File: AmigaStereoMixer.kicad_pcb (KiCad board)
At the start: 2 copper layers, 49.3 x 55.4 mm, 16 parts, among them J1 IN1_R, J2 IN1_L, J3 IN2_L, J4 IN2_R, J5 OUT_TRS

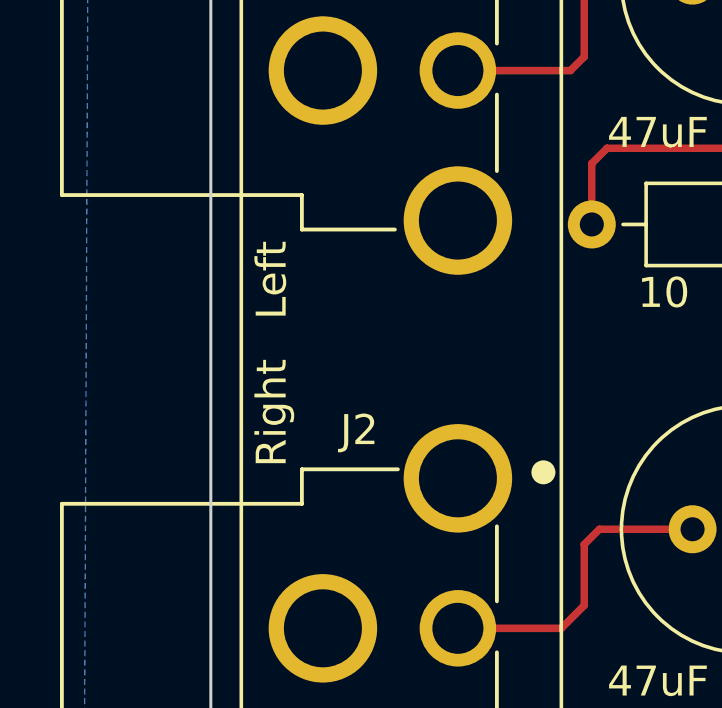
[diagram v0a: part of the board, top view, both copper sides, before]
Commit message: Arrange left & right groups more clearly in schema
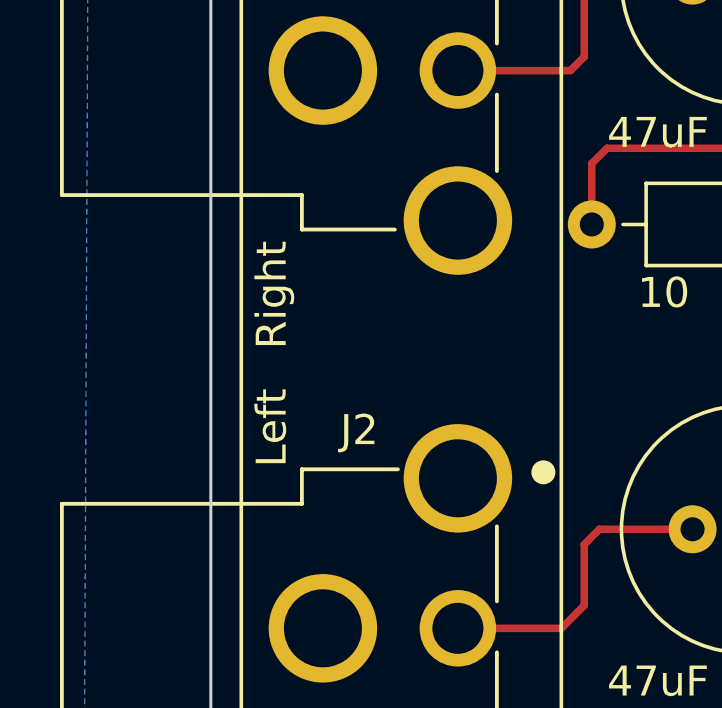
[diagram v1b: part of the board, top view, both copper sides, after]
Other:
- board text removed: "Right Left"
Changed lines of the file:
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@@
     (effects (font (size 1 1) (thickness 0.2)))
   )
-  (gr_text "Right   Left" (at 28.702 37.846 90) (layer F.SilkS)
+  (gr_text "Left   Right" (at 28.702 37.846 90) (layer F.SilkS)
     (effects (font (size 1 1) (thickness 0.2)))
   )

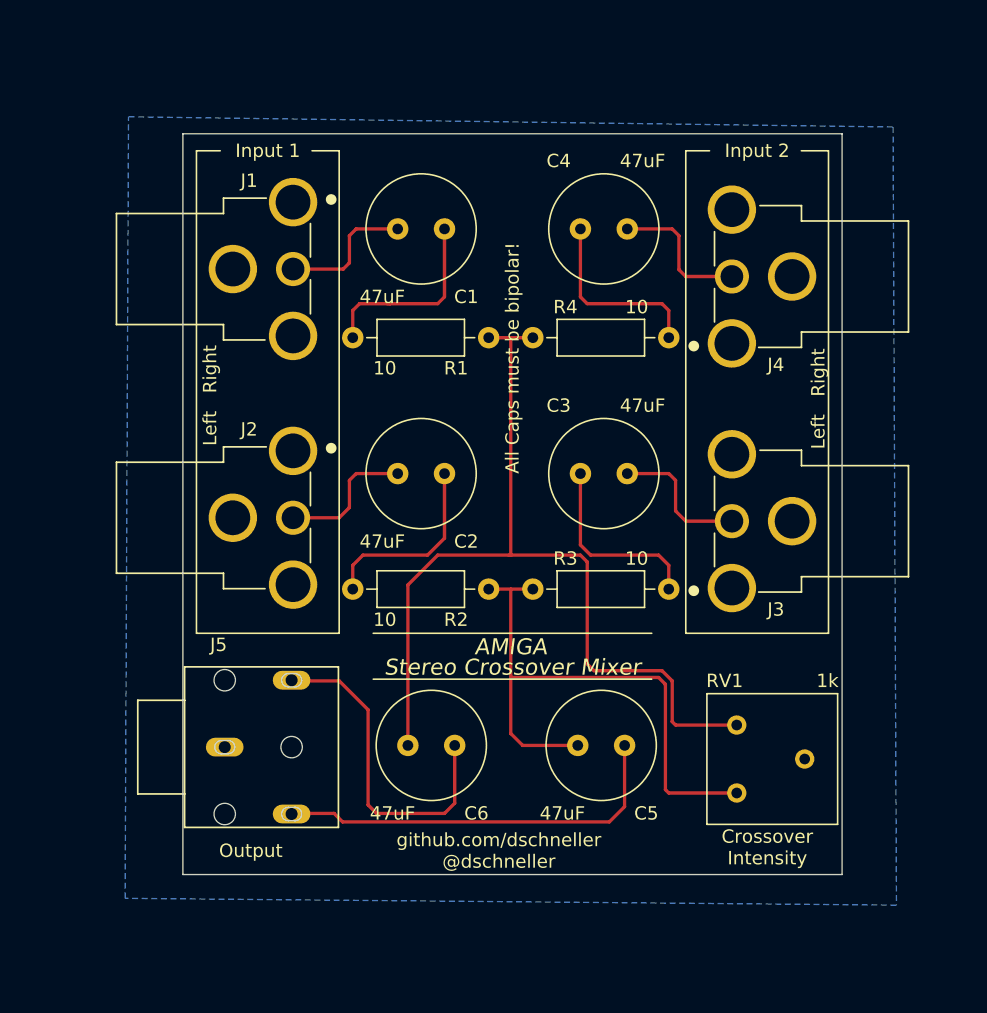
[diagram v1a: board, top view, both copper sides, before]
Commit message: Add mounting holes and an open hardware logo
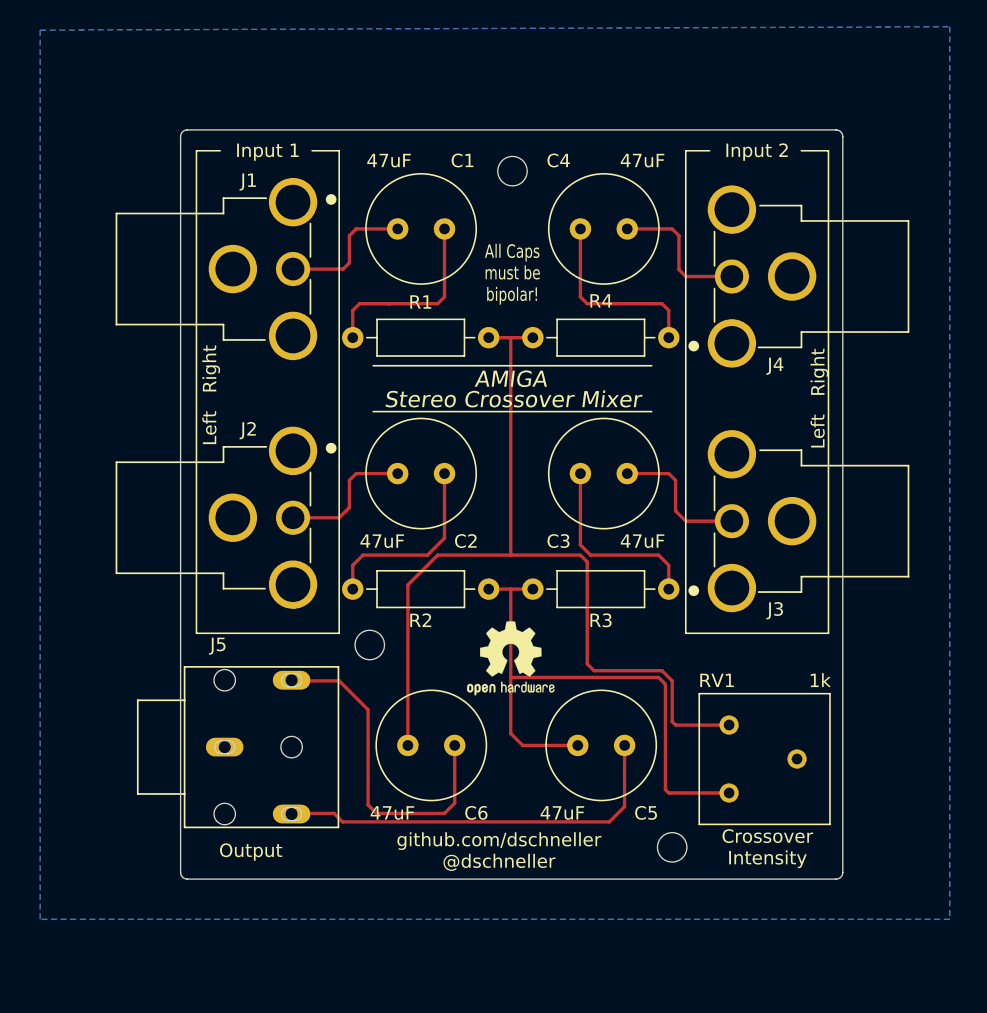
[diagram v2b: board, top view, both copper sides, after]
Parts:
- added H1: MountingHole, MountingHole:MountingHole_2.2mm_M2_DIN965, F.Cu at (51.3, 21.1)
- added H2: MountingHole, MountingHole:MountingHole_2.2mm_M2_DIN965, F.Cu at (63.2, 71.6)
- added H3: MountingHole, MountingHole:MountingHole_2.2mm_M2_DIN965, F.Cu at (40.6, 56.5)
- added REF**: OSHW-Logo2_7.3x6mm_SilkScreen, Symbol:OSHW-Logo2_7.3x6mm_SilkScreen, F.Cu at (51.2, 57.5)
- R1, R2, R3, R4: footprint AmigaStereoMixer:R_Axial_DIN0207_L6.3mm_D2.5mm_P10.16mm_Horizontal -> Resistor_THT:R_Axial_DIN0207_L6.3mm_D2.5mm_P10.16mm_Horizontal
- moved RV1 0.57 mm to (67.5, 67.6)
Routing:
- net Net-(C6-Pad2): track 68.6 -> 68.0 mm
- net Net-(C5-Pad2): track 44.6 -> 44.0 mm
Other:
- board size 49.3 x 55.4 mm -> 49.5 x 56 mm

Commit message: 0.5mm traces, Left/Right labels moved
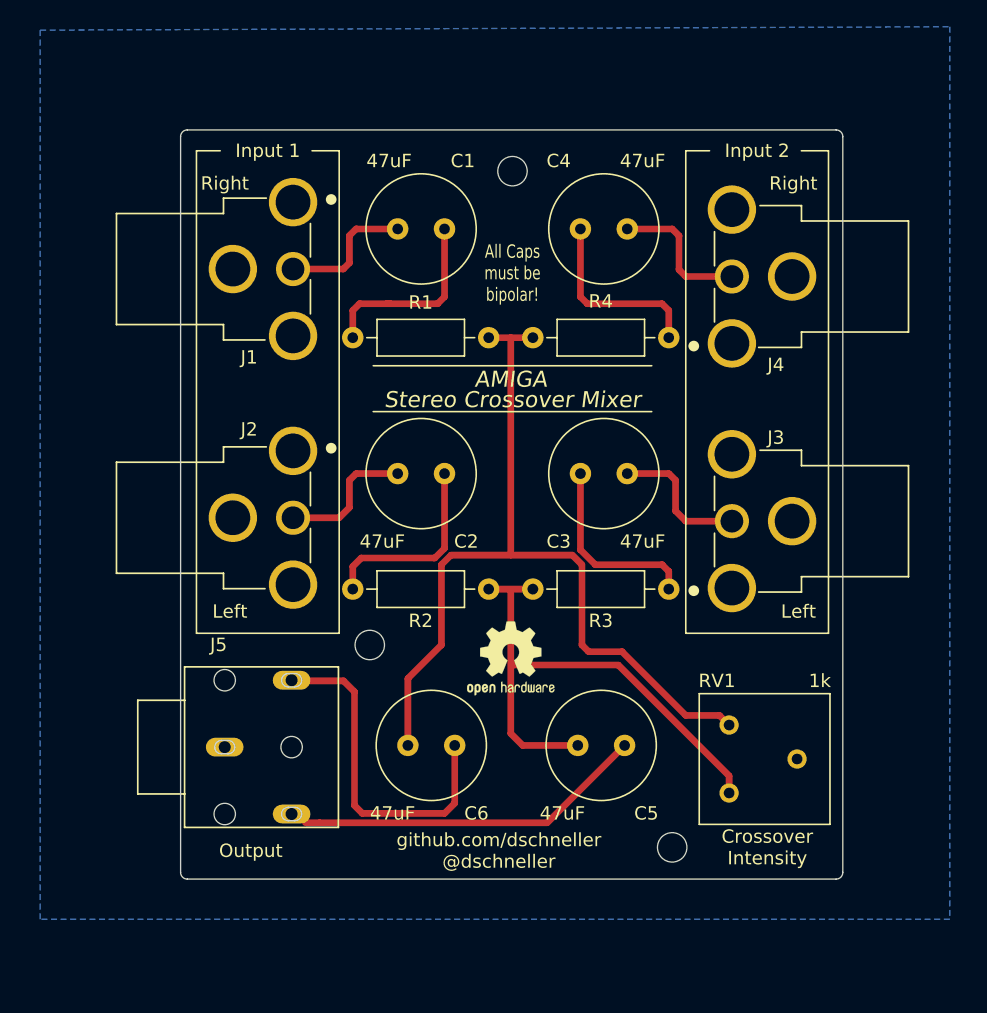
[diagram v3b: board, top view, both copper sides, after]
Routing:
- net Net-(C5-Pad2): track 44.0 -> 40.3 mm
- net Net-(C6-Pad2): track 68.0 -> 64.7 mm
- net Net-(C5-Pad1): track 28.8 -> 26.2 mm
- net Net-(C6-Pad1): track 23.7 -> 24.5 mm
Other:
- net class Default: trace_width 0.25 -> 0.5
- board text added: "Left"
- board text added: "Right"
- board text removed: "Left Right"

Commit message: Add front GND plane
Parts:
- moved J4 5.00 mm to (73.7, 34.0)
- moved C1 5.00 mm to (46.2, 30.4)
- moved C2 5.00 mm to (46.2, 48.7)
- moved C3 5.00 mm to (56.4, 48.7)
- moved C4 5.00 mm to (56.4, 30.4)
- moved C5 5.00 mm to (59.7, 69.0)
- moved C6 5.00 mm to (47.0, 69.0)
- moved H1 5.00 mm to (51.3, 26.1)
- moved H2 5.00 mm to (63.2, 76.6)
- moved H3 5.00 mm to (40.6, 61.5)
- moved J1 5.00 mm to (29.0, 33.4)
- moved J2 5.00 mm to (29.0, 52.0)
- moved J3 5.00 mm to (73.7, 52.2)
- moved J5 5.00 mm to (29.8, 69.1)
- moved R1 5.00 mm to (49.5, 38.5)
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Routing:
- added copper zone on F.Cu, net GND

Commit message: Improve some trace routing
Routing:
- net Net-(C5-Pad1): track 26.2 -> 29.2 mm
- net Net-(C5-Pad2): track 40.3 -> 41.9 mm
- net Net-(C6-Pad2): track 64.7 -> 64.1 mm
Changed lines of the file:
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@@
     (thickness 1.6)
     (drawings 34)
-    (tracks 73)
+    (tracks 76)
     (zones 0)
     (modules 20)
@@
   (segment (start 56.388 35.48) (end 56.896 35.988) (width 0.5) (layer F.Cu) (net 8))
   (segment (start 56.388 30.4) (end 56.388 35.48) (width 0.5) (layer F.Cu) (net 8))
-  (segment (start 59.69 69.008) (end 53.909989 74.788011) (width 0.5) (layer F.Cu) (net 9))
-  (segment (start 53.909989 74.788011) (end 36.895011 74.788011) (width 0.5) (layer F.Cu) (net 9))
-  (segment (start 36.895011 74.788011) (end 35.838174 74.788011) (width 0.5) (layer F.Cu) (net 9))
+  (segment (start 58.5 75) (end 36.050163 75) (width 0.5) (layer F.Cu) (net 9))
+  (segment (start 36.050163 75) (end 35.838174 74.788011) (width 0.5) (layer F.Cu) (net 9))
+  (segment (start 59.69 73.81) (end 58.5 75) (width 0.5) (layer F.Cu) (net 9))
+  (segment (start 59.69 69.008) (end 59.69 73.81) (width 0.5) (layer F.Cu) (net 9))
   (segment (start 49.53 57.324) (end 52.832 57.324) (width 0.5) (layer F.Cu) (net 10))
   (segment (start 52.07 69.008) (end 56.19 69.008) (width 0.5) (layer F.Cu) (net 10))
   (segment (start 51.181 57.324) (end 51.181 68.119) (width 0.5) (layer F.Cu) (net 10))
   (segment (start 51.181 68.119) (end 52.07 69.008) (width 0.5) (layer F.Cu) (net 10))
-  (segment (start 59.218 63) (end 51.362 63) (width 0.5) (layer F.Cu) (net 10))
-  (segment (start 67.5 71.282) (end 59.218 63) (width 0.5) (layer F.Cu) (net 10))
-  (segment (start 67.5 72.564) (end 67.5 71.282) (width 0.5) (layer F.Cu) (net 10))
+  (segment (start 59 63) (end 51.362 63) (width 0.5) (layer F.Cu) (net 10))
+  (segment (start 64.564 72.564) (end 64 72) (width 0.5) (layer F.Cu) (net 10))
+  (segment (start 64 68) (end 59 63) (width 0.5) (layer F.Cu) (net 10))
+  (segment (start 64 72) (end 64 68) (width 0.5) (layer F.Cu) (net 10))
+  (segment (start 67.5 72.564) (end 64.564 72.564) (width 0.5) (layer F.Cu) (net 10))
   (segment (start 49.53 38.528) (end 52.832 38.528) (width 0.5) (layer F.Cu) (net 11))
   (segment (start 51.181 38.528) (end 51.181 54.784) (width 0.5) (layer F.Cu) (net 11))
+  (segment (start 66.780001 66.764001) (end 67.5 67.484) (width 0.5) (layer F.Cu) (net 11))
+  (segment (start 46 56) (end 47.216 54.784) (width 0.5) (layer F.Cu) (net 11))
+  (segment (start 57 62) (end 59.5 62) (width 0.5) (layer F.Cu) (net 11))
   (segment (start 64.264001 66.764001) (end 66.780001 66.764001) (width 0.5) (layer F.Cu) (net 11))
-  (segment (start 57 62) (end 59.5 62) (width 0.5) (layer F.Cu) (net 11))
+  (segment (start 59.5 62) (end 64.264001 66.764001) (width 0.5) (layer F.Cu) (net 11))
+  (segment (start 46 61.5) (end 46 56) (width 0.5) (layer F.Cu) (net 11))
+  (segment (start 56.5 56) (end 56.5 61.5) (width 0.5) (layer F.Cu) (net 11))
+  (segment (start 43.49 64.01) (end 46 61.5) (width 0.5) (layer F.Cu) (net 11))
+  (segment (start 47.216 54.784) (end 55.284 54.784) (width 0.5) (layer F.Cu) (net 11))
+  (segment (start 55.284 54.784) (end 56.5 56) (width 0.5) (layer F.Cu) (net 11))
   (segment (start 56.5 61.5) (end 57 62) (width 0.5) (layer F.Cu) (net 11))
-  (segment (start 56.5 55.5) (end 56.5 61.5) (width 0.5) (layer F.Cu) (net 11))
-  (segment (start 59.5 62) (end 64.264001 66.764001) (width 0.5) (layer F.Cu) (net 11))
-  (segment (start 55.784 54.784) (end 56.5 55.5) (width 0.5) (layer F.Cu) (net 11))
-  (segment (start 46.716 54.784) (end 55.784 54.784) (width 0.5) (layer F.Cu) (net 11))
-  (segment (start 46 61.5) (end 46 55.5) (width 0.5) (layer F.Cu) (net 11))
-  (segment (start 66.780001 66.764001) (end 67.5 67.484) (width 0.5) (layer F.Cu) (net 11))
-  (segment (start 43.49 64.01) (end 46 61.5) (width 0.5) (layer F.Cu) (net 11))
-  (segment (start 46 55.5) (end 46.716 54.784) (width 0.5) (layer F.Cu) (net 11))
   (segment (start 43.49 69.008) (end 43.49 64.01) (width 0.5) (layer F.Cu) (net 11))
   (segment (start 38.682 64.182) (end 36.195 64.182) (width 0.5) (layer F.Cu) (net 12))
+  (segment (start 40 74) (end 39.5 73.5) (width 0.5) (layer F.Cu) (net 12))
+  (segment (start 46.316 74) (end 40 74) (width 0.5) (layer F.Cu) (net 12))
+  (segment (start 46.99 73.326) (end 46.316 74) (width 0.5) (layer F.Cu) (net 12))
+  (segment (start 39.5 73.5) (end 39.5 65) (width 0.5) (layer F.Cu) (net 12))
   (segment (start 39.5 65) (end 38.682 64.182) (width 0.5) (layer F.Cu) (net 12))
-  (segment (start 39.5 73.5) (end 39.5 65) (width 0.5) (layer F.Cu) (net 12))
-  (segment (start 46.228 74.088) (end 40.088 74.088) (width 0.5) (layer F.Cu) (net 12))
-  (segment (start 40.088 74.088) (end 39.5 73.5) (width 0.5) (layer F.Cu) (net 12))
-  (segment (start 46.99 73.326) (end 46.228 74.088) (width 0.5) (layer F.Cu) (net 12))
   (segment (start 46.99 69.008) (end 46.99 73.326) (width 0.5) (layer F.Cu) (net 12))
   (zone (net 13) (net_name GND) (layer B.Cu) (hatch edge 0.508)

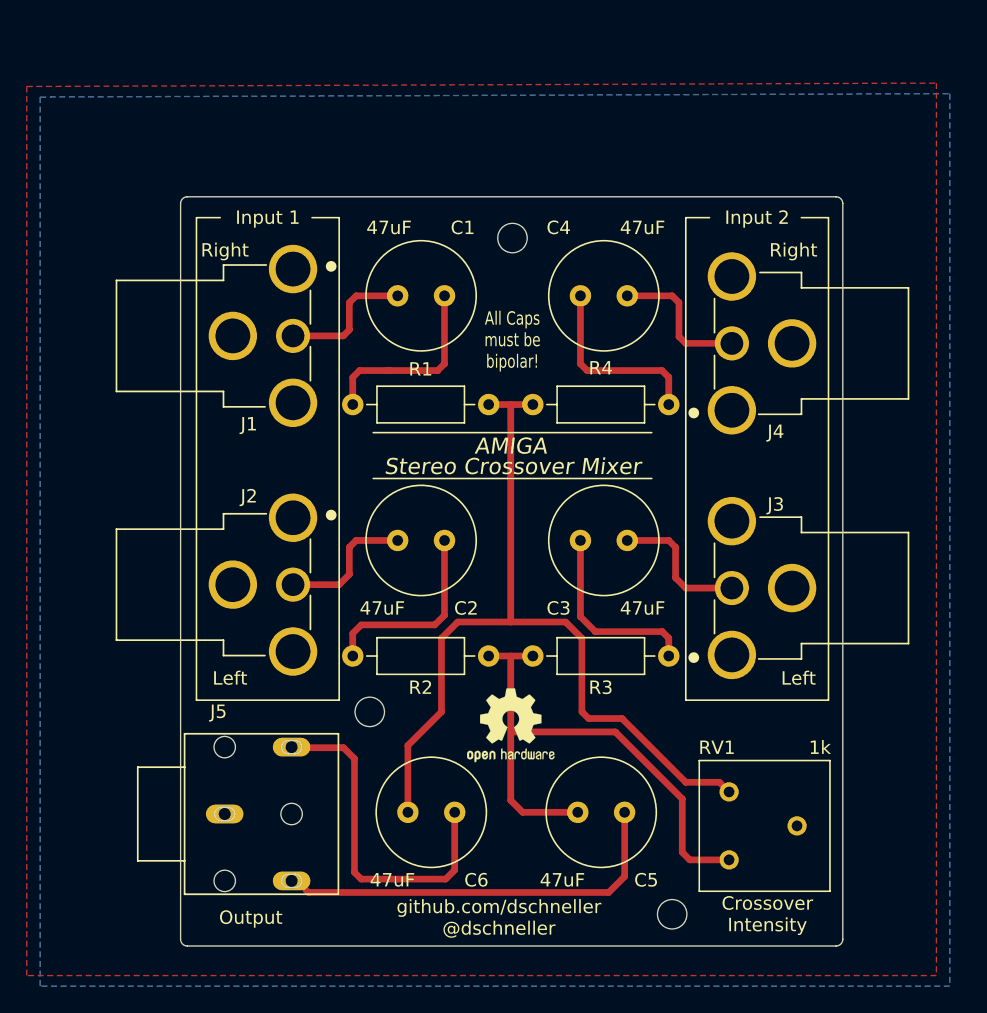
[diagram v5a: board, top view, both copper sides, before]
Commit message: Rev 2: Add missing connection, route on back
* Much more compact layout.
* The variable resistor was missing a link to its
  pin 2, rendering it practically useless.
* Update CUI symbols and footprints
  Use oval pad holes instead of board outline segments
  in SJ1-3553NG TRS output footprint.
* Enable previously missing backside solder mask
  and silk screen layers. Before the back was covered
  in 100% mask during manufacture, making it impossible
  to solder on the back side. This should now be fixed.
* Route tracks on the back of the board to make the
  front nicer and to make connections obvious when looking
  at the back.
* Update front solder mask texts
* Improve readme, add component names/part numbers.
* Add CERN OHL v1.2
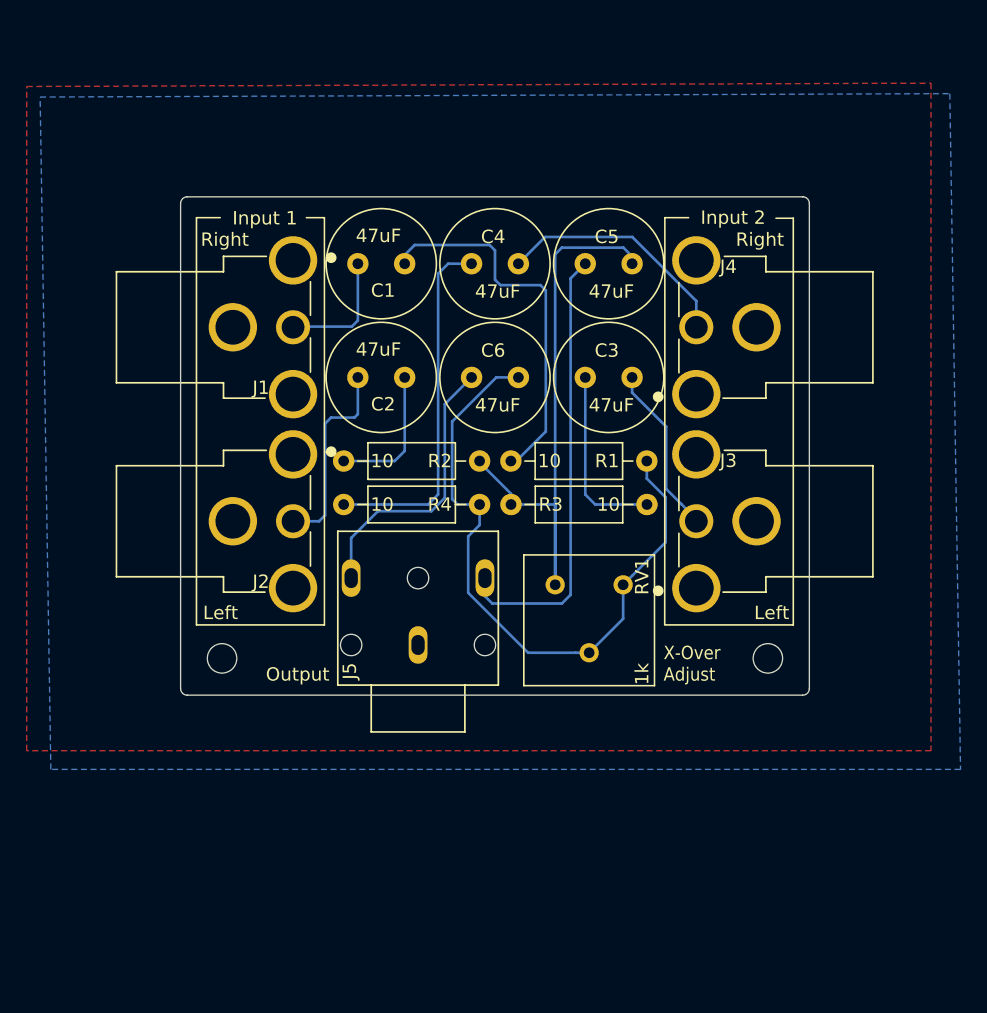
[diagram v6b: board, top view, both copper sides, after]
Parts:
- removed H3: MountingHole, MountingHole:MountingHole_2.2mm_M2_DIN965
- removed the REF** at (51.2, 62.5)
- added REF**: OSHW-Logo2_9.8x8mm_SilkScreen, Symbol:OSHW-Logo2_9.8x8mm_SilkScreen, B.Cu at (56.3, 45.3)
- R1, R2, R3, R4: footprint Resistor_THT:R_Axial_DIN0207_L6.3mm_D2.5mm_P10.16mm_Horizontal -> AmigaStereoMixer:R_Axial_DIN0207_L6.3mm_D2.5mm_P10.16mm_Horizontal
- moved C5 41.1 mm to (56.8, 28.0), turned to 0 degrees
- moved H1 38.2 mm to (29.6, 57.5)
- moved C6 32.5 mm to (48.2, 36.5), turned to 0 degrees
- moved RV1 24.3 mm to (54.5, 52.0), turned to 270 degrees
- moved H2 20.4 mm to (70.4, 57.5)
- moved J5 19.2 mm to (44.2, 56.5), turned to 90 degrees
- moved R2 14.6 mm to (48.9, 42.8)
- moved R1 12.6 mm to (61.4, 42.8)
- moved C2 12.5 mm to (43.2, 36.5)
- moved C3 12.2 mm to (56.8, 36.5)
- moved R3 11.4 mm to (51.2, 46.0)
- moved C4 8.48 mm to (48.2, 28.0)
- moved R4 8.47 mm to (48.9, 46.0), turned to 180 degrees
- moved J3 5.66 mm to (71.0, 47.2)
- moved J2 4.74 mm to (29.0, 47.2)
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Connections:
- RV1 pad 2: (no net) -> Net-(C6-Pad2)
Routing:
- net Net-(C6-Pad2): track 64.1 -> 49.5 mm
- net Net-(C1-Pad1): track 14.6 -> 28.3 mm
- net Net-(C4-Pad1): track 14.1 -> 26.5 mm
- net Net-(C4-Pad2): track 10.8 -> 18.1 mm
- net Net-(C2-Pad2): track 10.1 -> 14.9 mm
- net Net-(C2-Pad1): track 14.7 -> 10.4 mm
- net Net-(C5-Pad1): track 29.2 -> 33.5 mm
- net Net-(C6-Pad1): track 24.4 -> 21.1 mm
- net Net-(C5-Pad2): track 41.9 -> 45.0 mm
- net Net-(C3-Pad2): track 10.6 -> 12.8 mm
- net Net-(C1-Pad2): track 10.3 -> 8.73 mm
- net Net-(C3-Pad1): track 14.3 -> 13.6 mm
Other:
- board size 49.5 x 56 mm -> 47 x 37.2 mm
- net class Default: trace_width 0.5 -> 0.2; via_dia 0.8 -> 0.6
- board text added: "CERN Open Hardware Licence v1.2"
- board text added: "X-Over Adjust"
- board text added: "github.com/dschneller :: @dschneller"
- board text added: "rev2"
- board text removed: "Crossover Intensity"
- board text removed: "github.com/dschneller @dschneller"
